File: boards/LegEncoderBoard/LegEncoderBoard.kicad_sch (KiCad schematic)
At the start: 38 parts, among them J1 Conn_01x05, Q1 MMBT3904, Q2 MMBT3904, Q3 MMBT3904, U1 AS5047P-ATST, U2 SN74LVC3G17DCUR

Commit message: Wrong schematic title
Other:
- title: Upper Arm Encoder Board -> Leg (Wheel) Encoder Board
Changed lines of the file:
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@@
 	(paper "A4")
 	(title_block
-		(title "Upper Arm Encoder Board")
+		(title "Leg (Wheel) Encoder Board")
 		(company "01 Binary")
 	)

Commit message: Prepare encoder boards for manufacturing
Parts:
- C1: footprint Capacitor100nF:885342208002 -> Capacitor100nF:CC0603KRX7R9BB104; LCSC C2176910 -> C14663
- C2: LCSC C2169542 -> C85973
- R6: LCSC (none) -> C114608
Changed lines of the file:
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@@
 			)
 		)
-		(property "Footprint" "Capacitor100nF:885342208002"
+		(property "Footprint" "Capacitor100nF:CC0603KRX7R9BB104"
 			(at 144.78 49.53 0)
 			(effects
@@
 			)
 		)
-		(property "LCSC" "C2176910"
+		(property "LCSC" "C14663"
 			(at 147.32 48.3869 0)
 			(effects
@@
 			)
 		)
+		(property "LCSC" "C114608"
+			(at 224.79 76.2 0)
+			(effects
+				(font
+					(size 1.27 1.27)
+				)
+				(hide yes)
+			)
+		)
 		(pin "1"
 		)
@@
 			)
 		)
-		(property "LCSC" "C2169542"
+		(property "LCSC" "C85973"
 			(at 160.02 48.3869 0)
 			(effects

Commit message: Pre-flight on two encoder boards
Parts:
- C2: footprint Capacitor10nF:885012206089 -> Capacitor10nF:GRM1885C1H103JA01D
- C4: value 0.1uF -> 100nF; footprint Capacitor0.1uF:GRM188R71H104KA93J -> Capacitor100nF:CC0603KRX7R9BB104; LCSC (none) -> C14663
- D1: footprint RedLED:RC0603FR-07150RL -> LedRed:YLED0603R
- D2, D3: footprint BlueLED:150080BS75000_Modified -> LedBlue:YLED0603B
- R13, R14, R15: LCSC C105579 -> C107701
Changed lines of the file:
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@@
 			)
 		)
-		(property "LCSC" "C105579"
+		(property "LCSC" "C107701"
 			(at 137.16 175.26 0)
 			(effects
@@
 			)
 		)
-		(property "LCSC" "C105579"
+		(property "LCSC" "C107701"
 			(at 129.54 177.8 0)
 			(effects
@@
 			)
 		)
-		(property "Footprint" "BlueLED:150080BS75000_Modified"
+		(property "Footprint" "LedBlue:YLED0603B"
 			(at 201.93 109.22 0)
 			(effects
@@
 			)
 		)
-		(property "Value" "0.1uF"
+		(property "Value" "100nF"
 			(at 246.38 34.4169 0)
 			(effects
@@
 			)
 		)
-		(property "Footprint" "Capacitor0.1uF:GRM188R71H104KA93J"
+		(property "Footprint" "Capacitor100nF:CC0603KRX7R9BB104"
 			(at 243.84 33.02 0)
 			(effects
@@
 			)
 		)
+		(property "LCSC" "C14663"
+			(at 246.38 31.8769 0)
+			(effects
+				(font
+					(size 1.27 1.27)
+				)
+				(hide yes)
+			)
+		)
 		(pin "2"
 		)
@@
 			)
 		)
-		(property "LCSC" "C105579"
+		(property "LCSC" "C107701"
 			(at 144.78 172.72 0)
 			(effects
@@
 			)
 		)
-		(property "Footprint" "RedLED:RC0603FR-07150RL"
+		(property "Footprint" "LedRed:YLED0603R"
 			(at 201.93 137.16 0)
 			(effects
@@
 			)
 		)
-		(property "Footprint" "BlueLED:150080BS75000_Modified"
+		(property "Footprint" "LedBlue:YLED0603B"
 			(at 201.93 82.55 0)
 			(effects
@@
 			)
 		)
-		(property "Footprint" "Capacitor10nF:885012206089"
+		(property "Footprint" "Capacitor10nF:GRM1885C1H103JA01D"
 			(at 157.48 49.53 0)
 			(effects

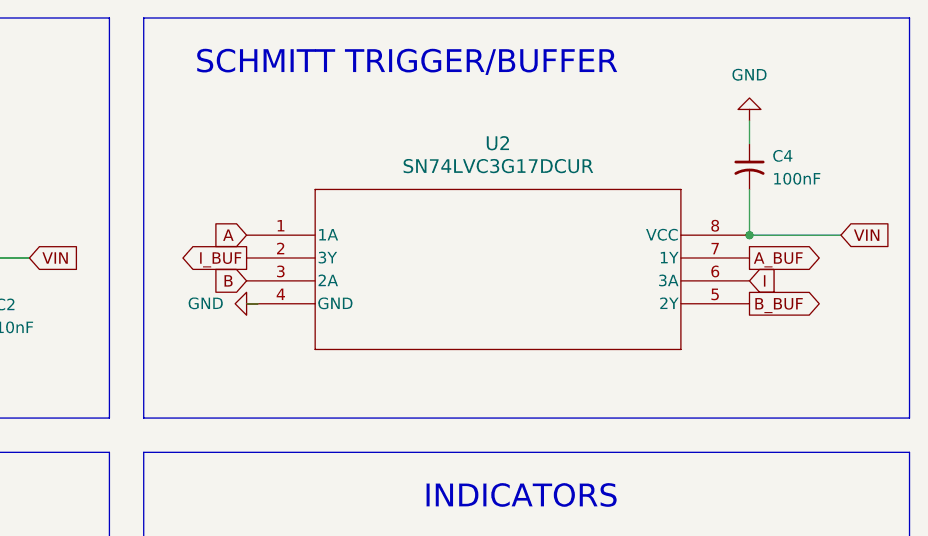
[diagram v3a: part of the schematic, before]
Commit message: Ordered leg encoder board
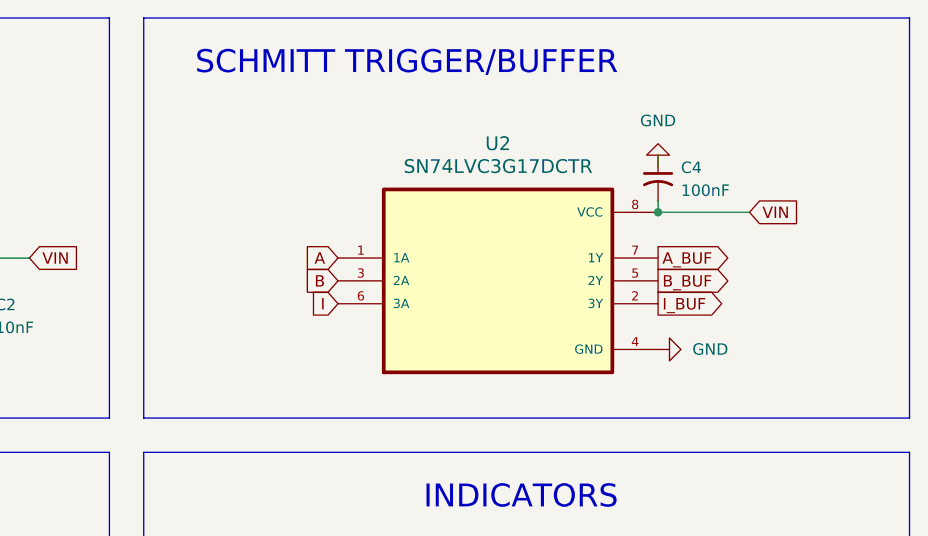
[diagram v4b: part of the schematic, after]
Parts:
- D1: footprint LedRed:YLED0603R -> LedRed:NCD0603R1
- D2, D3: footprint LedBlue:YLED0603B -> LedBlue:150080BS75000_Modified
- U2: value SN74LVC3G17DCUR -> SN74LVC3G17DCTR; footprint SchmittBuffer:SN74LVC3G17DCUR -> SchmittBuffer:SN74LVC3G17DCTR; symbol SchmittBuffer:SN74LVC3G17DCUR -> SchmittBuffer:SN74LVC3G17DCTRE4; Availability (none) -> In Stock; Check_prices (none) -> https://www.snapeda.com/parts/SN74LVC3G17DCTRE4/Texas+Instr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; Description_1 (none) -> TRIPLE SCHMITT-TRIGGER BUFFER 8-SM8 -40 to 125; DigiKey_Part_Number (none) -> 296-18818-1-ND; LCSC C68245 -> C18213; MANUFACTURER (none) -> Texas Instruments; MAXIMUM_PACKAGE_HEIGHT (none) -> 0.9 mm; MF (none) -> Texas Instruments; MP (none) -> SN74LVC3G17DCTRE4; PARTREV (none) -> F; Package (none) -> SSOP-8 Texas Instruments; Price (none) -> None; STANDARD (none) -> IPC-7351B; SnapEDA_Link (none) -> https://www.snapeda.com/parts/SN74LVC3G17DCTRE4/Texas+Instr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
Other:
- moved on the sheet: C4

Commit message: Finalize leg encoder board iteration
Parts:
- added C10, C8, C9: 10nF, Capacitor10nF:GRM1885C1H103JA01D, symbol Device:C_Small_US
- added CR4, CR5, CR6: BAT54, EnvelopeDiode:BAT54WS-7-F, symbol EnvelopeDiode:BAT54WS-7-F
- added J2: Conn_01x04, Connector_JST:JST_XH_B4B-XH-A_1x04_P2.50mm_Vertical, symbol Connector_Generic:Conn_01x04
- added R16, R17, R18: 100K, Resistor100K:CRCW0603100KFKEA, symbol Device:R_US
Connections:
- net A: now also U1.7 (A); no longer U1.6 (B)
- net A_BUF: now also C8.1; no longer CR1.2
- net B: now also U1.6 (B); no longer U1.7 (A)
- net B_BUF: now also C9.1; no longer CR2.2
- net GND: now also CR4.2, CR5.2, CR6.2, R16.2, R17.2, R18.2; no longer U1.2 (CLK), U1.4 (MOSI)
- net I_BUF: now also C10.1; no longer CR3.2
- net VIN: no longer U1.1 (CSn)
- net MISO: now reaches U1.3 (MISO)
- net MISO: now also J2.3 (Pin_3)
- new net A_PULSE: C8.2, CR1.2, CR4.1, R16.1
- new net B_PULSE: C9.2, CR2.2, CR5.1, R17.1
- new net CLK: J2.2 (Pin_2), U1.2 (CLK)
- new net CS: J2.1 (Pin_1), U1.1 (CSn)
- new net I_PULSE: C10.2, CR3.2, CR6.1, R18.1
- new net MOSI: J2.4 (Pin_4), U1.4 (MOSI)
- no-connect marks 4 -> 3
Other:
- moved on the sheet: C1, C2, C3, C4, C5, C6, C7, CR1, CR2, CR3, D1, D2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

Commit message: Debug and re-design leg encoder and leg robot board
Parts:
- removed C10: 10nF, Capacitor10nF:GRM1885C1H103JA01D, symbol Device:C_Small_US
- removed CR6: BAT54, EnvelopeDiode:BAT54WS-7-F, symbol EnvelopeDiode:BAT54WS-7-F
- removed R18: 100K, Resistor100K:CRCW0603100KFKEA, symbol Device:R_US
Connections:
- net I_PULSE is gone; now on net I_BUF: CR3.2
